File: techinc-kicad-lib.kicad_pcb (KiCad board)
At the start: 2 copper layers, 0 parts

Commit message: add esp-12/-07/-08
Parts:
- added D1: SAMSUNG_RGB_LED_5050_SPMFCT5606N0S0A1E0, 5050RGB_LED, F.Cu at (48.4, 26.9)
- added IC1: WS2801, SO14E, F.Cu at (46.1, 36.9)
- added IC2: MAX490, SO8E, F.Cu at (67.3, 62.4)
- added IC3: WS2811, SO8E, F.Cu at (54.1, 68.8)
- added U1: ESP-01, ESP-01, F.Cu at (26.1, 70.0)
- added U2: ESP-03, ESP-03, F.Cu at (24.1, 28.0)
- added U3: WS2812, WS2812, F.Cu at (83.1, 68.2)
- added U4: WS2812B, WS2812B, F.Cu at (67.9, 72.5)
- added U5: ESP-12, ESP-12, F.Cu at (63.4, 43.0)
- added U6: ESP-07, ESP-07, F.Cu at (91.3, 30.8)
- added U7: ESP-08, ESP-08, F.Cu at (91.3, 51.6)

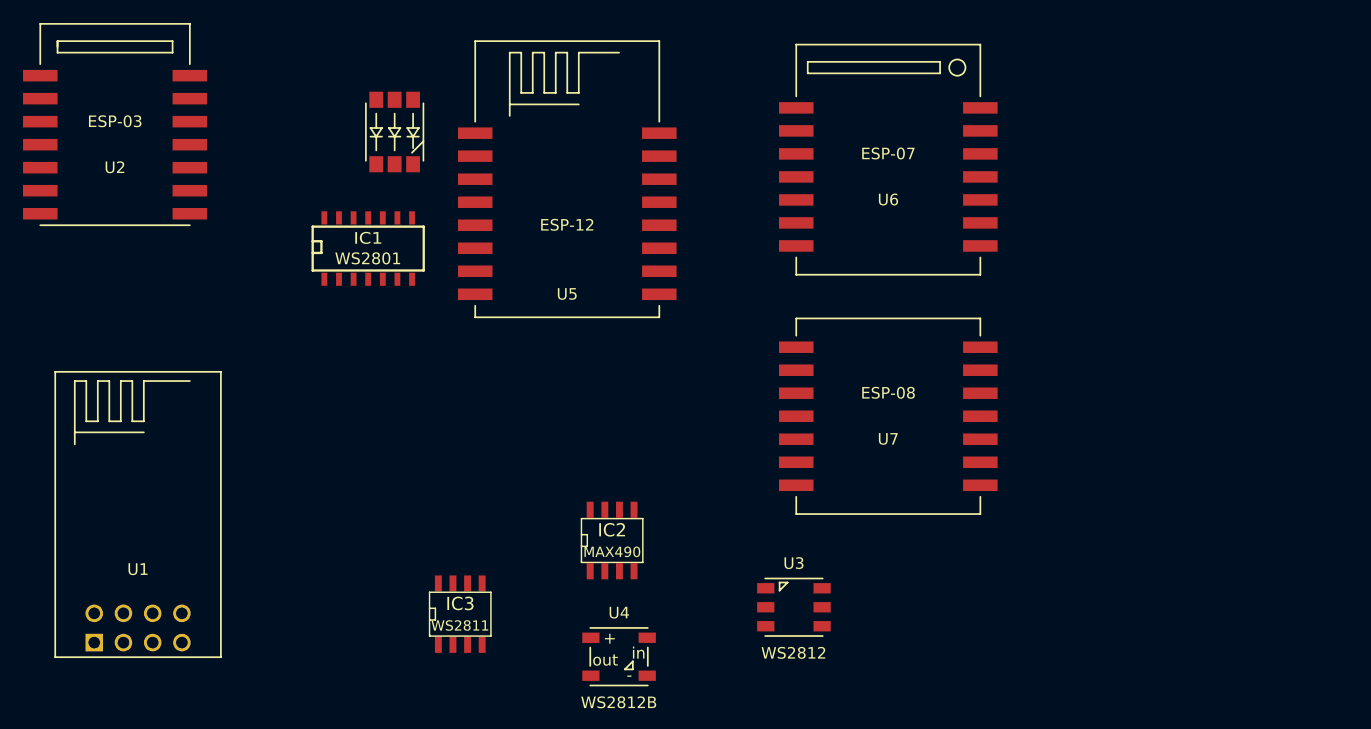
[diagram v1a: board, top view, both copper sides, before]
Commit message: add esp-07v2/08v2
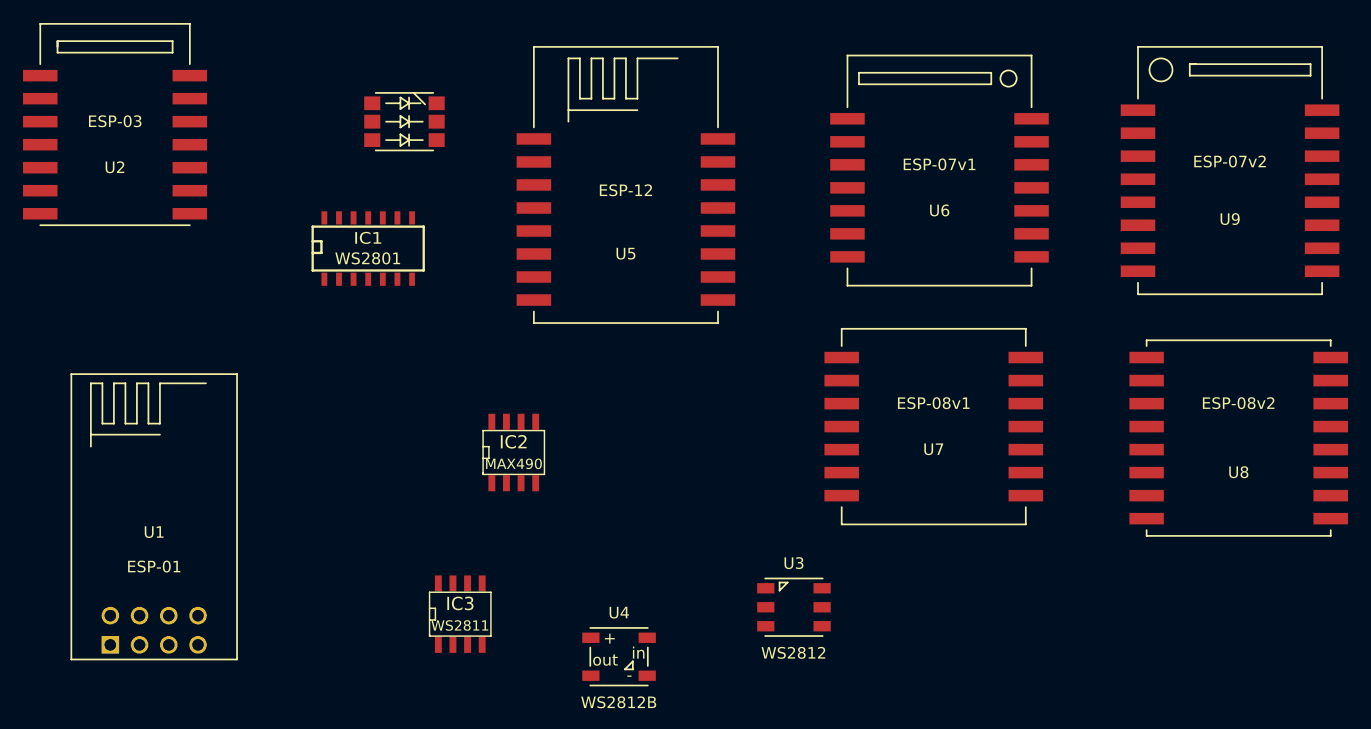
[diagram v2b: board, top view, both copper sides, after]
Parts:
- added U8: ESP-08v2, ESP-08v2, F.Cu at (121.8, 53.5)
- added U9: ESP-07v2, ESP-07v2, F.Cu at (121.0, 32.0)
- U6: value ESP-07 -> ESP-07v1; footprint ESP-07 -> ESP-07v1
- U7: value ESP-08 -> ESP-08v1; footprint ESP-08 -> ESP-08v1
- moved IC2 11.5 mm to (58.8, 54.8)
- moved U5 9.91 mm to (68.5, 34.5)
- moved U6 4.55 mm to (95.8, 31.8)
- moved U7 4.05 mm to (95.2, 52.5)
- moved U1 1.41 mm to (27.5, 70.2)
- moved D1 1.24 mm to (49.2, 26.0), turned to 90 degrees

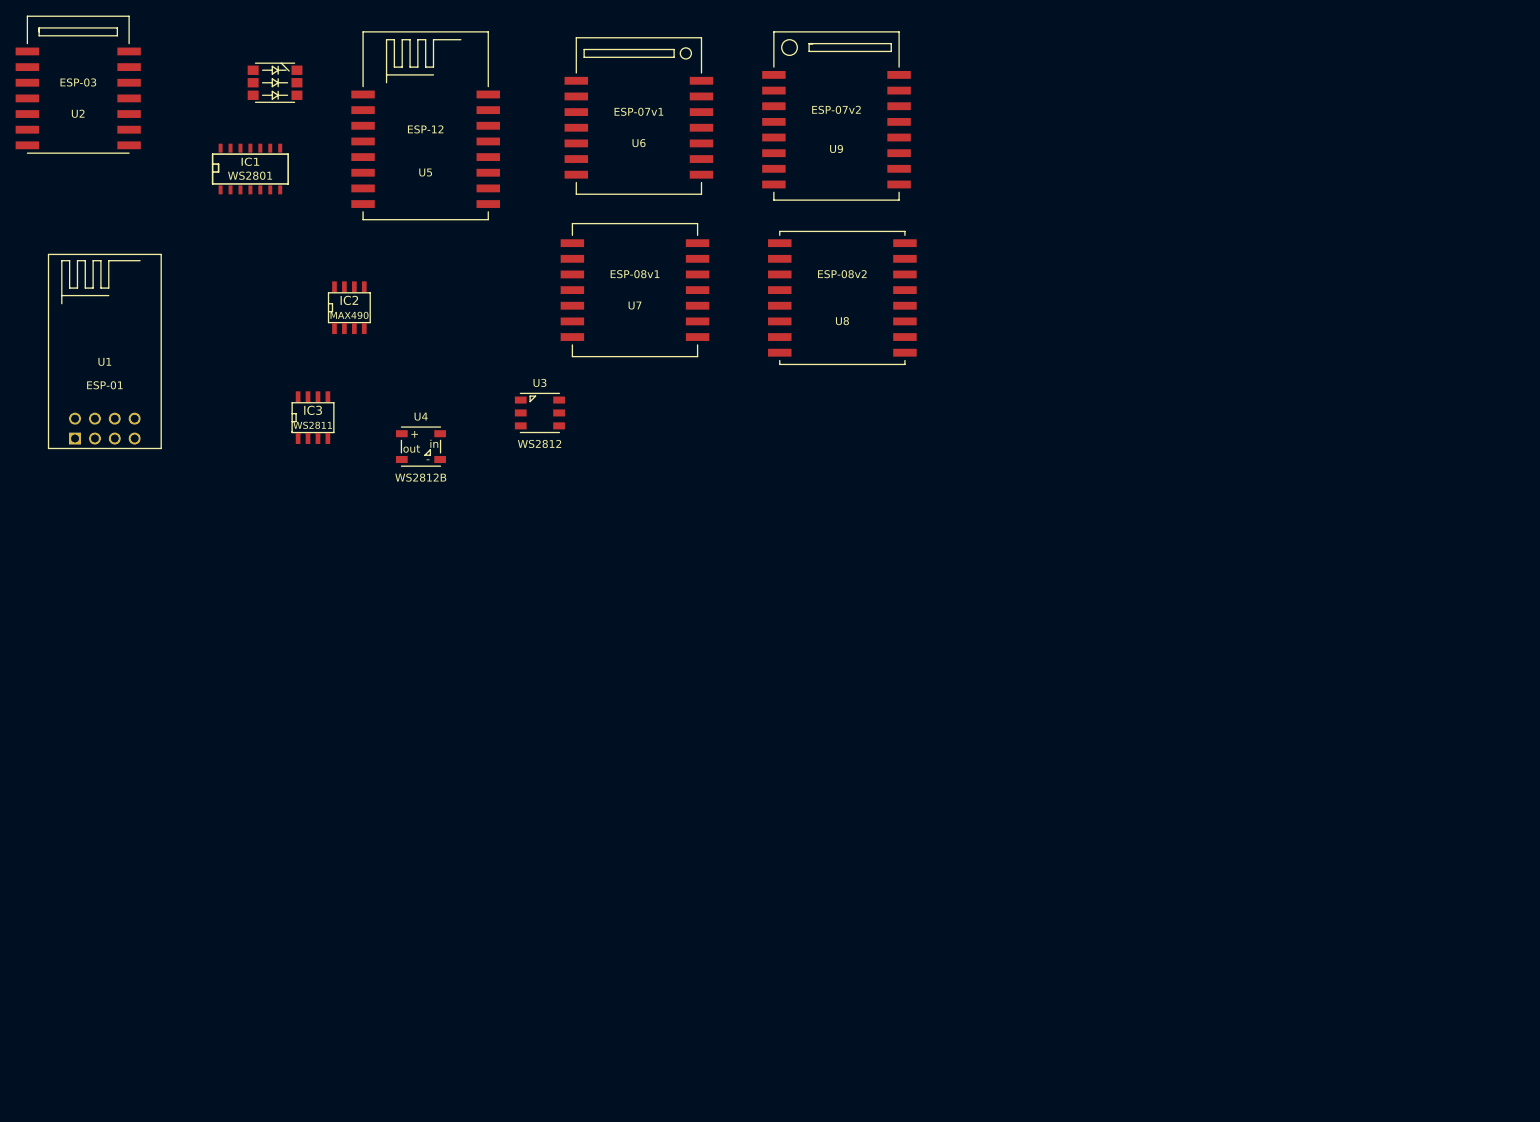
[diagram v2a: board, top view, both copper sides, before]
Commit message: add arduino shield modules
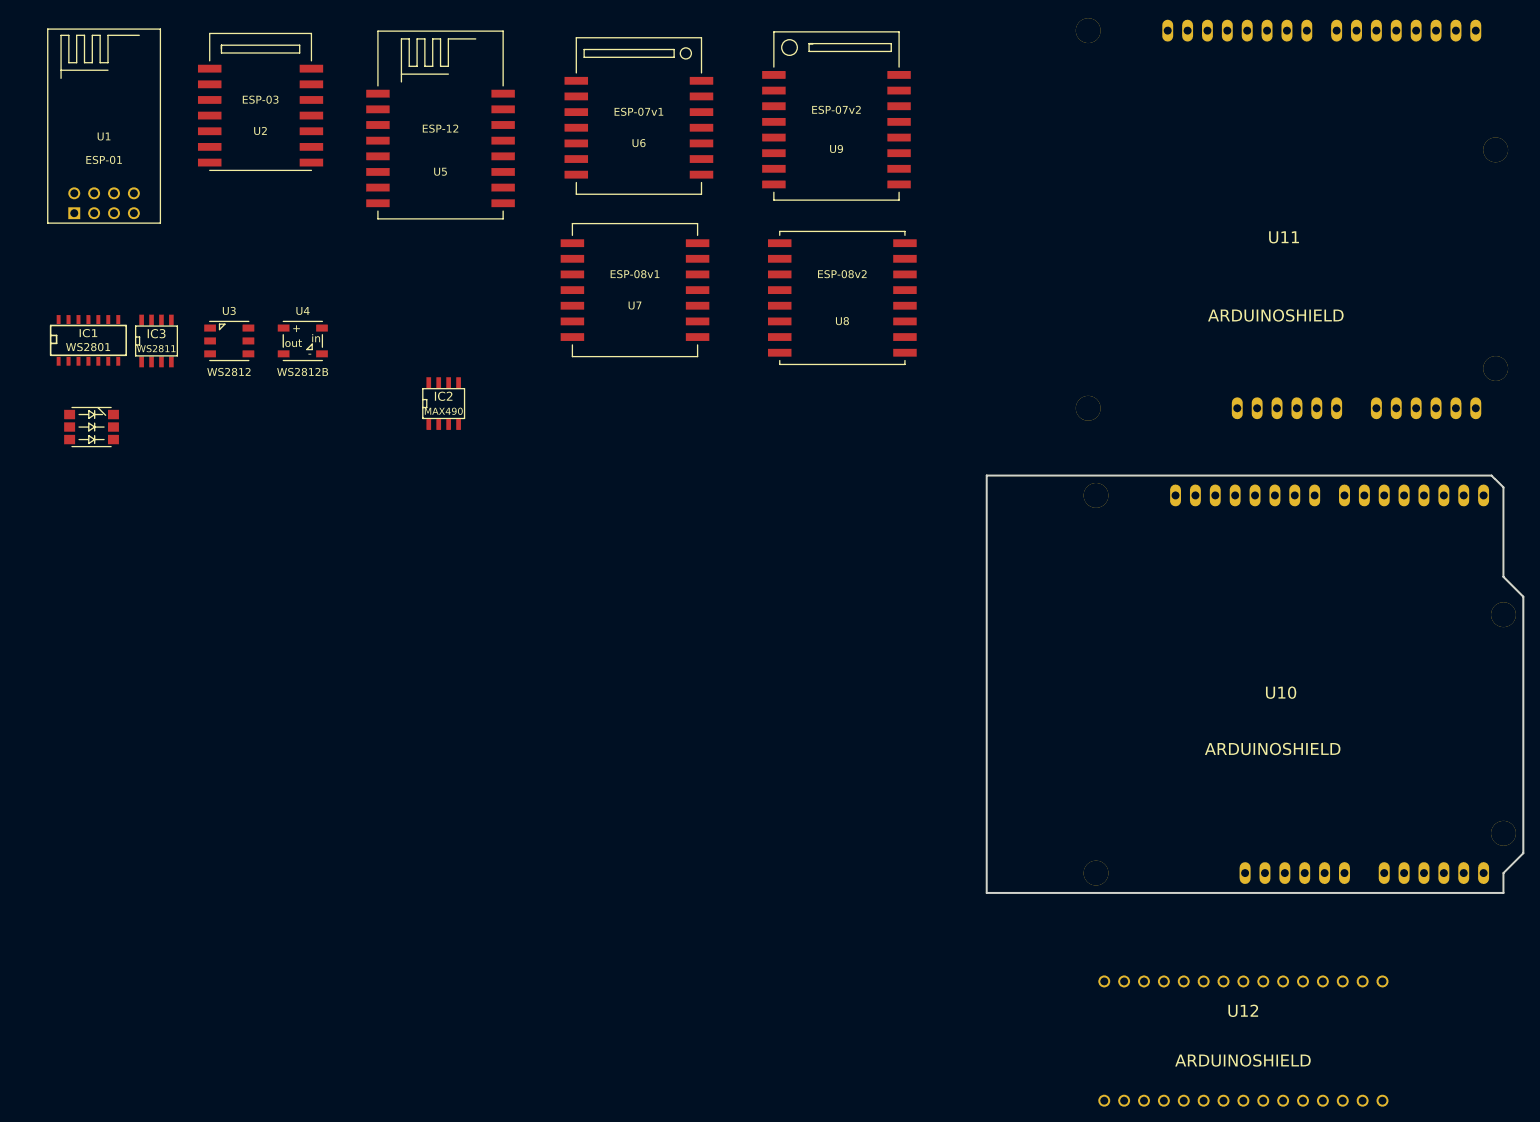
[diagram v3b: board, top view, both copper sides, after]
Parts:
- added U10: ARDUINOSHIELD, arduinoshield, F.Cu at (140.2, 76.2)
- added U11: ARDUINOSHIELD, arduinoshield_no_edges, F.Cu at (139.2, 16.8)
- added U12: ARDUINOSHIELD, nanoshield_no_edges, F.Cu at (173.0, 147.2)
- moved D1 49.9 mm to (25.8, 70.0)
- moved U3 40.8 mm to (43.4, 59.0)
- moved IC1 30.1 mm to (25.4, 58.8)
- moved U1 28.8 mm to (27.4, 41.4)
- moved U2 23.4 mm to (47.4, 30.2)
- moved IC3 22.3 mm to (34.1, 59.0)
- moved U4 20.3 mm to (52.8, 59.0)
- moved IC2 17.2 mm to (70.8, 67.0)
- moved U5 1.90 mm to (70.4, 34.4)
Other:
- board outline added: 68.6 x 53.3 mm

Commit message: add NH-14 nixie tube lib/footprint
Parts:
- added U13: NH-14, NH-14, F.Cu at (32.0, 90.6)
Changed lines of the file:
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@@
     (tracks 0)
     (zones 0)
-    (modules 16)
+    (modules 17)
     (nets 1)
   )
@@
       (layers *.Cu *.Mask F.SilkS)
     )
+  )
+  (module NH-14 (layer F.Cu)
+    (at 32 90.6)
+    (fp_text reference U13 (at 0 -7.5) (layer F.SilkS)
+      (effects (font (size 1 1) (thickness 0.15)))
+    )
+    (fp_text value NH-14 (at 0 8) (layer F.SilkS)
+      (effects (font (size 1 1) (thickness 0.15)))
+    )
+    (fp_line (start -0.2 3) (end 0.2 3) (layer F.SilkS) (width 0.15))
+    (fp_line (start 0.2 3) (end 0.2 -1.6) (layer F.SilkS) (width 0.15))
+    (fp_line (start 0.2 -1.6) (end 1.2 -1.6) (layer F.SilkS) (width 0.15))
+    (fp_line (start 1.2 -1.6) (end 0 -3.6) (layer F.SilkS) (width 0.15))
+    (fp_line (start 0 -3.6) (end -1 -1.6) (layer F.SilkS) (width 0.15))
+    (fp_line (start -1 -1.6) (end -0.2 -1.6) (layer F.SilkS) (width 0.15))
+    (fp_line (start -0.2 -1.6) (end -0.2 3) (layer F.SilkS) (width 0.15))
+    (fp_circle (center 0 0) (end 0 -9) (layer F.SilkS) (width 0.15))
+    (pad 1 thru_hole oval (at 0 -5.5) (size 1.25 2.5) (drill 1)
+      (layers *.Cu *.Mask F.SilkS)
+    )
+    (pad 2 thru_hole oval (at 2.556 -4.87 332.3) (size 1.25 2.5) (drill 1)
+      (layers *.Cu *.Mask F.SilkS)
+    )
+    (pad 3 thru_hole oval (at 4.526 -3.124 304.6) (size 1.25 2.5) (drill 1)
+      (layers *.Cu *.Mask F.SilkS)
+    )
+    (pad 4 thru_hole oval (at 5.46 -0.663 276.9) (size 1.25 2.5) (drill 1)
+      (layers *.Cu *.Mask F.SilkS)
+    )
+    (pad 5 thru_hole oval (at 5.143 1.95 249.2) (size 1.25 2.5) (drill 1)
+      (layers *.Cu *.Mask F.SilkS)
+    )
+    (pad 6 thru_hole oval (at 3.647 4.117 221.5) (size 1.25 2.5) (drill 1)
+      (layers *.Cu *.Mask F.SilkS)
+    )
+    (pad 7 thru_hole oval (at 1.316 5.34 193.8) (size 1.25 2.5) (drill 1)
+      (layers *.Cu *.Mask F.SilkS)
+    )
+    (pad 8 thru_hole oval (at -1.316 5.34 166.1) (size 1.25 2.5) (drill 1)
+      (layers *.Cu *.Mask F.SilkS)
+    )
+    (pad 9 thru_hole oval (at -3.647 4.117 138.4) (size 1.25 2.5) (drill 1)
+      (layers *.Cu *.Mask F.SilkS)
+    )
+    (pad 10 thru_hole oval (at -5.143 1.95 110.7) (size 1.25 2.5) (drill 1)
+      (layers *.Cu *.Mask F.SilkS)
+    )
+    (pad 11 thru_hole oval (at -5.46 -0.663 83) (size 1.25 2.5) (drill 1)
+      (layers *.Cu *.Mask F.SilkS)
+    )
+    (pad 12 thru_hole oval (at -4.526 -3.124 55.3) (size 1.25 2.5) (drill 1)
+      (layers *.Cu *.Mask F.SilkS)
+    )
+    (pad 13 thru_hole oval (at -2.556 -4.87 27.6) (size 1.25 2.5) (drill 1)
+      (layers *.Cu *.Mask F.SilkS)
+    )

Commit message: rename nixie tube component/lib
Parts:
- U13: value NH-14 -> IN-14; footprint NH-14 -> IN-14
- moved U13 1.90 mm to (32.6, 88.8)
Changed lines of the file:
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@@
     )
   )
-  (module NH-14 (layer F.Cu)
-    (at 32 90.6)
+  (module IN-14 (layer F.Cu)
+    (at 32.6 88.8)
     (fp_text reference U13 (at 0 -7.5) (layer F.SilkS)
       (effects (font (size 1 1) (thickness 0.15)))
     )
-    (fp_text value NH-14 (at 0 8) (layer F.SilkS)
+    (fp_text value IN-14 (at 0 8) (layer F.SilkS)
       (effects (font (size 1 1) (thickness 0.15)))
     )
